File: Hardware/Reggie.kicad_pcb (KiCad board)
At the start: 4 copper layers, 70 x 50 mm, 223 parts, among them IC1 ADS131M04IRUKR, IC2 TPS61089RNRR, IC3 AP2205-W5-7, IC4 AP2205-W5-7, IC5 TPS61089RNRR, J1 RBUS, J2 USB_C_Receptacle_USB2.0, J3 ServoConnector1, J4 1053131104, J5 1053131104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

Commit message: Overall Routing Complete!!!
Version2
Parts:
- C76, C77, C78, C79, C80, C81: moved to B.Cu
- moved C81 81.2 mm to (130.8, 80.3), turned to 180 degrees
- moved C80 80.4 mm to (130.8, 78.0), turned to 180 degrees
- moved C79 79.5 mm to (130.8, 75.7), turned to 180 degrees
- moved C78 78.6 mm to (130.8, 73.4), turned to 180 degrees
- moved C76 77.8 mm to (130.8, 71.0), turned to 0 degrees
- moved TC1 61.8 mm to (184.7, 70.9), turned to 0 degrees
- moved TC2 58.7 mm to (178.0, 65.0), turned to 90 degrees
- moved R39 57.5 mm to (182.7, 71.8), turned to 90 degrees
- moved R40 57.2 mm to (182.7, 73.8), turned to 90 degrees
- moved C34 56.6 mm to (181.8, 69.5), turned to 180 degrees
- moved R42 56.0 mm to (178.9, 67.2), turned to 180 degrees
- moved C31 55.8 mm to (181.7, 71.0), turned to -90 degrees
- moved C38 55.6 mm to (180.1, 68.1), turned to 0 degrees
- moved C32 55.3 mm to (181.7, 72.8), turned to -90 degrees
- moved C77 55.3 mm to (124.5, 100.0), turned to 180 degrees
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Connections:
- D6 pad 3: /GPIO13 -> /GPIO2
- D6 pad 4: /GPIO14 -> /GPIO1
- D6 pad 6: /GPIO16 -> /GPIO14
- D6 pad 7: /GPIO39 -> /GPIO13
- J8 pad 2: /GPIO4 -> /GPIO1
- J8 pad 3: /GPIO13 -> /GPIO2
- J8 pad 4: /GPIO14 -> /GPIO13
- J8 pad 6: /GPIO15 -> /GPIO14
- J8 pad 7: /GPIO16 -> /GPIO4
- J8 pad 8: /GPIO39 -> /GPIO15
- U1 pad 22: /GPIO16 -> unconnected-(U1-GPIO16/ADC2_CH5/XTAL_32K_N-Pad22)
- U1 pad 44: /GPIO39 -> unconnected-(U1-MTCK/JTAG/GPIO39-Pad44)
- U1 pad 6: unconnected-(U1-GPIO1/ADC1_CH0-Pad6) -> /GPIO1
- U1 pad 7: unconnected-(U1-GPIO2/ADC1_CH1-Pad7) -> /GPIO2
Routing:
- net /HSPI_MOSI: track 0.00 -> 83.3 mm, vias 0 -> 4
- net /HSPI_MISO: track 0.00 -> 75.2 mm, vias 0 -> 4
- net /HSPI_SCLK: track 0.00 -> 68.6 mm, vias 0 -> 4
- net +6V: track 0.00 -> 62.5 mm, vias 0 -> 1
- net /T_DRDY1: track 0.00 -> 45.0 mm, vias 0 -> 2
- net +5V: track 0.00 -> 40.4 mm, vias 0 -> 4
- net /T_CS1: track 0.00 -> 39.5 mm, vias 0 -> 2
- net +12V: track 0.00 -> 37.8 mm, vias 0 -> 5
- net /T_FAULT1: track 0.00 -> 35.4 mm, vias 0 -> 2
- net /ADS_CS: track 0.00 -> 34.3 mm, vias 0 -> 2
- net /SD_DET: track 0.00 -> 34.0 mm, vias 0 -> 2
- net /CHIP_PU: track 10.7 -> 43.8 mm
- net /GPIO15: track 0.00 -> 32.2 mm, vias 0 -> 2
- net /CAN+: track 7.68 -> 39.6 mm
- net Net-(C6-Pad1): track 4.26 -> 35.7 mm
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- added copper zone on B.Cu, net +6V
- added copper zone on F.Cu, net +6V
- added copper zone on F.Cu, net /Buck/SW
- added copper zone on F.Cu, net /Sensor Power/LDO12V_IN
- added copper zone on F.Cu, net /Sensor Power/LDO5.5V_IN
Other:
- board text added: "3"

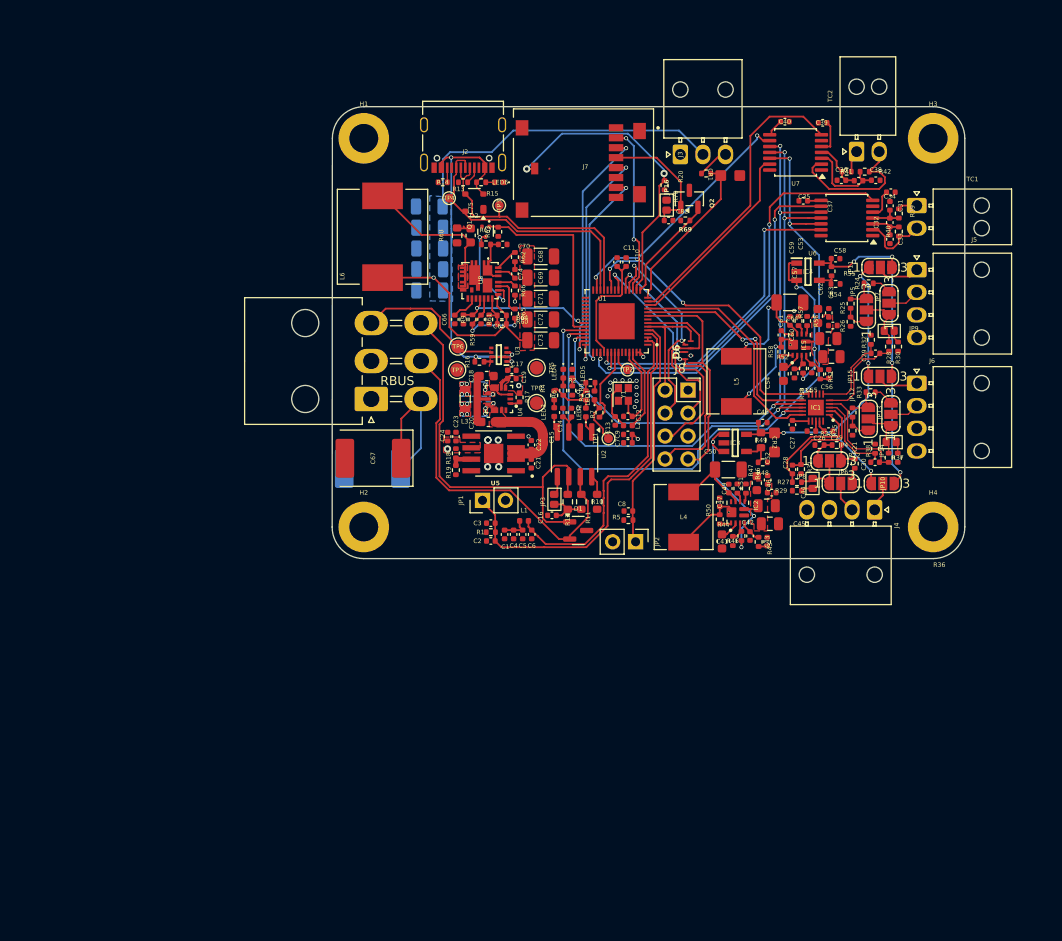
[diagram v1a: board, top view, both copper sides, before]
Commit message: Routing Improvement
Version 3. Mainly solved 3 problem: 1. clock and decoupler closer to microcontroller; 2. Route of Data+ and Data- neater; 3. wider trace for 6v and 16.8v
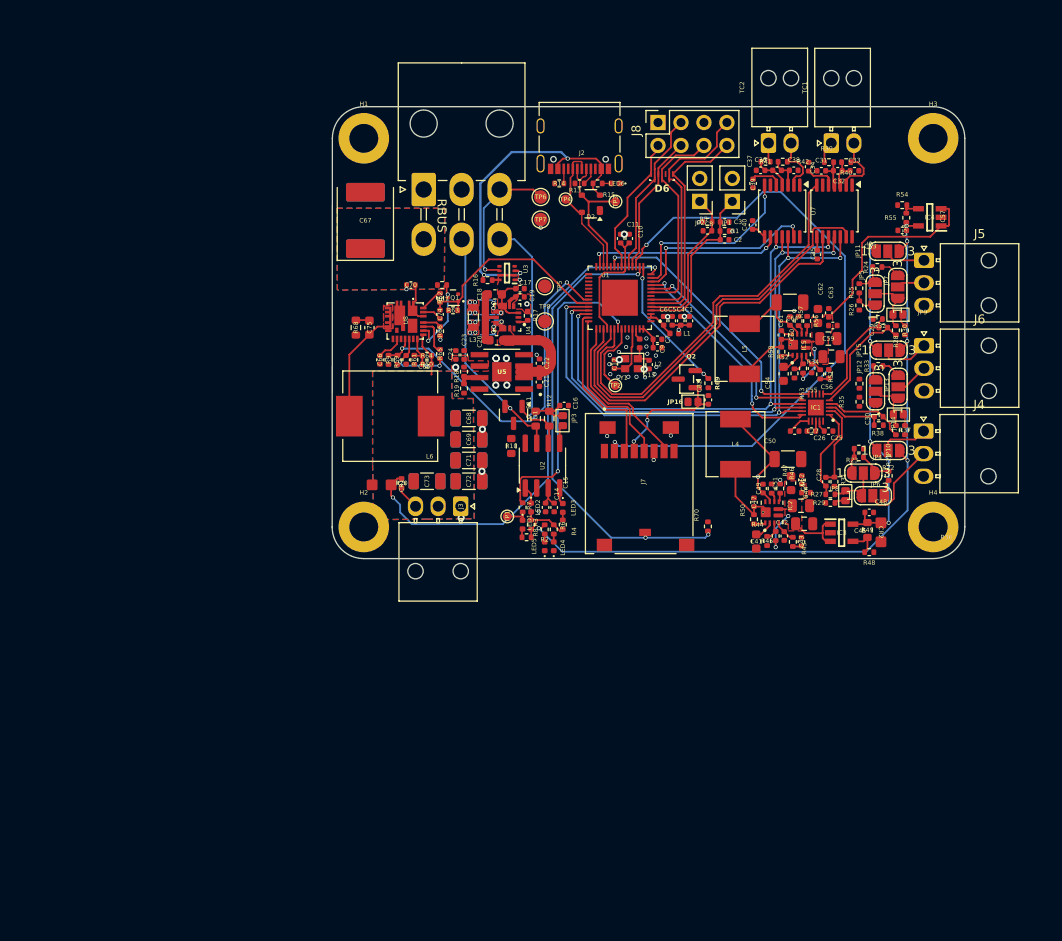
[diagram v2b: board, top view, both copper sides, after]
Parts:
- J4, J5, J6: footprint Connector_Molex:Molex_Nano-Fit_105313-xx04_1x04_P2.50mm_Horizontal -> Connector_Molex:Molex_Nano-Fit_105313-xx03_1x03_P2.50mm_Horizontal
- moved CR1 51.6 mm to (125.5, 101.8), turned to 180 degrees
- moved R20 48.1 mm to (127.7, 101.7), turned to -90 degrees
- moved J3 45.9 mm to (134.2, 104.2), turned to -90 degrees
- moved JP1 43.1 mm to (164.3, 70.5), turned to 180 degrees
- moved C3 42.2 mm to (163.4, 72.8), turned to 0 degrees
- moved R1 42.2 mm to (163.4, 73.8), turned to 180 degrees
- moved C2 42.2 mm to (163.4, 74.7), turned to 0 degrees
- moved JP2 38.3 mm to (160.7, 70.5), turned to 180 degrees
- moved R70 38.1 mm to (161.6, 106.4), turned to 90 degrees
- moved J7 36.2 mm to (154.0, 101.9), turned to -90 degrees
- moved R5 34.2 mm to (161.5, 72.7)
- moved C8 32.2 mm to (161.5, 73.7)
- moved C1 31.3 mm to (159.5, 83.7), turned to 90 degrees
- moved C76 30.4 mm to (130.5, 101.4)
- moved C4 30.0 mm to (158.6, 83.7), turned to 90 degrees
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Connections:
- D6 pad 1: /GPIO4 -> /GPIO1
- D6 pad 3: /GPIO2 -> /GPIO13
- D6 pad 4: /GPIO1 -> /GPIO15
- D6 pad 5: /GPIO15 -> /GPIO2
- D6 pad 6: /GPIO14 -> /GPIO4
- D6 pad 7: /GPIO13 -> /GPIO14
- J8 pad 2: /GPIO1 -> /GPIO15
- J8 pad 3: /GPIO2 -> /GPIO14
- J8 pad 6: /GPIO14 -> /GPIO4
- J8 pad 7: /GPIO4 -> /GPIO2
- J8 pad 8: /GPIO15 -> /GPIO1
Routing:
- net +6V: track 62.5 -> 4.88 mm, vias 1 -> 0
- net /SD_CS: track 19.0 -> 71.9 mm
- net +12V: track 37.8 -> 82.7 mm
- net /ServoPWM: track 18.1 -> 57.4 mm, vias 0 -> 2
- net Net-(C6-Pad1): track 35.7 -> 3.36 mm
- net Net-(U1-U0TXD/PROG/GPIO43): track 8.41 -> 33.8 mm, vias 0 -> 2
- net /CHIP_PU: track 43.8 -> 18.7 mm
- net /BuckPGOOD: track 16.1 -> 41.1 mm
- net /SD_DET: track 34.0 -> 51.9 mm, vias 2 -> 3
- net /HSPI_MOSI: track 83.3 -> 66.2 mm
- net +16.8V: track 22.4 -> 5.46 mm
- net /GPIO15: track 32.2 -> 15.7 mm, vias 2 -> 0
- net /CAN-: track 44.2 -> 28.4 mm, vias 0 -> 1
- net /Data+: track 30.6 -> 15.7 mm
- net /Data-: track 30.1 -> 16.9 mm
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- added copper zone on B.Cu, net +16.8V
- added copper zone on F.Cu, net +16.8V

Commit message: Filled zones and via location
Version 4. allocate filled zones and vias, also reassigned pins from microcontroller
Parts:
- C75, R68: moved to B.Cu
- moved TP8 19.5 mm to (146.5, 103.0)
- moved TP5 18.8 mm to (138.5, 98.0)
- moved R18 18.1 mm to (137.9, 107.1)
- moved C24 18.1 mm to (137.0, 105.2)
- moved R16 18.1 mm to (140.6, 96.9)
- moved U3 18.1 mm to (142.7, 96.2)
- moved C17 18.1 mm to (144.1, 97.9)
- moved C18 18.1 mm to (141.4, 98.5)
- moved C19 18.1 mm to (144.1, 98.8)
- moved C20 18.1 mm to (141.5, 103.6)
- moved C21 18.1 mm to (146.3, 108.2)
- moved C22 18.1 mm to (146.3, 106.1)
- moved C23 18.1 mm to (138.0, 105.2)
- moved L3 18.1 mm to (139.0, 101.1)
- moved R17 18.1 mm to (145.0, 100.9)
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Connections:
- D2 pad 2: VBUS -> /Data-
- D2 pad 3: /Data- -> VBUS
- D6 pad 1: /GPIO1 -> /TVS1
- D6 pad 3: /GPIO13 -> /TVS3
- D6 pad 4: /GPIO15 -> /TVS4
- D6 pad 5: /GPIO2 -> /TVS5
- D6 pad 6: /GPIO4 -> /TVS6
- D6 pad 7: /GPIO14 -> /TVS7
- J8 pad 2: /GPIO15 -> /TVS4
- J8 pad 3: /GPIO14 -> /TVS7
- J8 pad 4: /GPIO13 -> /TVS3
- J8 pad 6: /GPIO4 -> /TVS6
- J8 pad 7: /GPIO2 -> /TVS5
- J8 pad 8: /GPIO1 -> /TVS1
- R7 pad 2: Net-(U1-U0TXD/PROG/GPIO43) -> Net-(U1-SPICLK_P/GPIO47)
- U1 pad 11: /ADS_CLK -> /ADS_CS
- U1 pad 12: /T_FAULT0 -> /T_CS0
- U1 pad 13: /T_DRDY0 -> /T_FAULT0
- U1 pad 14: /ServoPWM -> /T_CS1
- U1 pad 15: /SD_EN -> /T_FAULT1
- U1 pad 16: /SD_DET -> /T_DRDY1
- U1 pad 17: /SD_CS -> /T_DRDY0
- U1 pad 18: /GPIO13 -> /TVS1
- U1 pad 19: /GPIO14 -> /TVS5
- U1 pad 21: /GPIO15 -> /TVS6
- U1 pad 22: unconnected-(U1-GPIO16/ADC2_CH5/XTAL_32K_N-Pad22) -> /TVS3
- U1 pad 23: /ADS_CS -> /TVS7
- U1 pad 24: unconnected-(U1-GPIO18/ADC2_CH7/DAC_1-Pad24) -> /TVS4
- U1 pad 27: /T_CS0 -> /BUCK_EN
- U1 pad 37: /BUCK_EN -> Net-(U1-SPICLK_P/GPIO47)
- U1 pad 41: /VSPI_MOSI -> /SD_CS
- U1 pad 42: /VSPI_SCLK -> /VSPI_MOSI
- U1 pad 43: /VSPI_MISO -> /VSPI_SCLK
- U1 pad 45: /T_CS1 -> unconnected-(U1-MTDO/JTAG/GPIO40-Pad45)
- U1 pad 47: /T_FAULT1 -> /VSPI_MISO
- U1 pad 48: /T_DRDY1 -> /SD_EN
- U1 pad 49: Net-(U1-U0TXD/PROG/GPIO43) -> /SD_DET
- U1 pad 6: /GPIO1 -> unconnected-(U1-GPIO1/ADC1_CH0-Pad6)
- U1 pad 7: /GPIO2 -> /ServoPWM
- U1 pad 9: /GPIO4 -> /ADS_CLK
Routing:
- net /SD_CS: track 71.9 -> 20.5 mm, vias 2 -> 0
- net Net-(U1-U0TXD/PROG/GPIO43): track 33.8 -> 0.00 mm, vias 2 -> 0
- net /GPIO2: track 27.9 -> 0.00 mm
- net /GPIO1: track 25.5 -> 0.00 mm
- net /GPIO4: track 23.0 -> 0.00 mm
- net /TVS5: track 0.00 -> 22.1 mm
- net VBUS: track 37.2 -> 59.0 mm
- net RBUS_uC_V: track 16.2 -> 37.1 mm
- net /T_DRDY1: track 45.6 -> 25.7 mm
- net /TVS1: track 0.00 -> 19.4 mm
- net /TVS7: track 0.00 -> 19.0 mm
- net Net-(U1-SPICLK_P/GPIO47): track 0.00 -> 18.4 mm
- net /TVS6: track 0.00 -> 18.4 mm
- net /GPIO14: track 18.3 -> 0.00 mm
- net /T_CS1: track 42.9 -> 25.5 mm
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- added copper zone on In2.Cu, net +3V3
- added copper zone on B.Cu, net GND
- added copper zone on In1.Cu, net GND

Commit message: via improvement and footprint allocation
Version 4.1
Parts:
- moved JP2 2.46 mm to (161.1, 77.2)
- moved C34 2.40 mm to (172.7, 69.0)
- moved C40 1.90 mm to (166.4, 76.4)
- moved R39 1.90 mm to (175.0, 68.0)
- moved R40 1.90 mm to (176.9, 68.0)
- moved TC1 1.90 mm to (175.2, 65.9)
- moved TC2 1.90 mm to (168.3, 65.9)
- moved C31 1.90 mm to (174.1, 69.0)
- moved C32 1.90 mm to (175.9, 69.0)
- moved C33 1.90 mm to (177.8, 69.0)
- moved C36 1.90 mm to (167.4, 68.9)
- moved C37 1.90 mm to (169.2, 68.9)
- moved C38 1.90 mm to (171.1, 68.9)
- moved C39 1.90 mm to (166.6, 70.4)
- moved R41 1.90 mm to (168.0, 68.0)
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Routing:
- net +16.8V: track 14.2 -> 10.7 mm, vias 0 -> 16
- net /Buck/PHASE: track 0.00 -> 2.06 mm
- net /T_CS0: track 19.8 -> 17.8 mm
- net +3V3: track 59.5 -> 61.5 mm, vias 22 -> 24
- net /ServoPWM: track 57.6 -> 59.5 mm
- net /T_FAULT0: track 23.1 -> 21.2 mm
- net /T_DRDY0: track 20.4 -> 18.5 mm
- net /HSPI_SCLK: track 60.5 -> 58.6 mm
- net /HSPI_MOSI: track 66.4 -> 64.5 mm
- net /HSPI_MISO: track 63.7 -> 61.8 mm
- net /T_DRDY1: track 25.7 -> 23.8 mm
- net /T_FAULT1: track 28.1 -> 26.2 mm
- net /T_CS1: track 25.5 -> 23.6 mm
- net /Buck/BOOT: track 0.00 -> 1.88 mm
- net Net-(J4-Pin_2): track 3.67 -> 5.21 mm
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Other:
- board text added: "J3"
